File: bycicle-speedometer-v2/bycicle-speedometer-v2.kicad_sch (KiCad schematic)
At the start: 2 parts, among them J1 Conn_01x04_Pin

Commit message: initiated schematic update
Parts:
- removed uP1: ProMini2, Pro mini:Pro_Mini, symbol j_ProcessorBoards:ProMini2
- added C1: C, symbol Device:C
- added R1, R2, R3, R4, R5: R, symbol Device:R
- added U1: ESP-12E, ESP8266:ESP-12E, symbol ESP8266:ESP-12E
- J1: footprint Display:Adafruit_SSD1306 -> Connector_PinSocket_2.54mm:PinSocket_1x04_P2.54mm_Vertical
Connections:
- new net GND: C1.2, R5.2, U1.9 (GND)

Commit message: modified schematic
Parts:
- removed R4: R, symbol Device:R
- added J2: Conn_01x02_Pin, symbol Connector:Conn_01x02_Pin
- added SW1: SW_Push_Dual, symbol Switch:SW_Push_Dual
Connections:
- net GND: now also J1.4 (Pin_4), J2.1 (Pin_1), SW1.1
- net at U1.1 (REST): now also R2.2, SW1.2
- net at U1.10 (GPIO15): now also R5.1
- net Prog: now reaches U1.12 (GPIO0)
- net Prog: now also R3.2, J2.2 (Pin_2)
- net SDA: now reaches U1.13 (GPIO4)
- net SDA: now also J1.1 (Pin_1)
- net SCL: now reaches U1.14 (GPIO5)
- net SCL: now also J1.2 (Pin_2)
- net at U1.3 (CH_PD): now also R1.2
- net at U1.8 (VCC): now also C1.1
- net VCC: now reaches R2.1
- net VCC: now also J1.3 (Pin_3), R1.1, R3.1
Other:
- moved on the sheet: C1, R1, R5

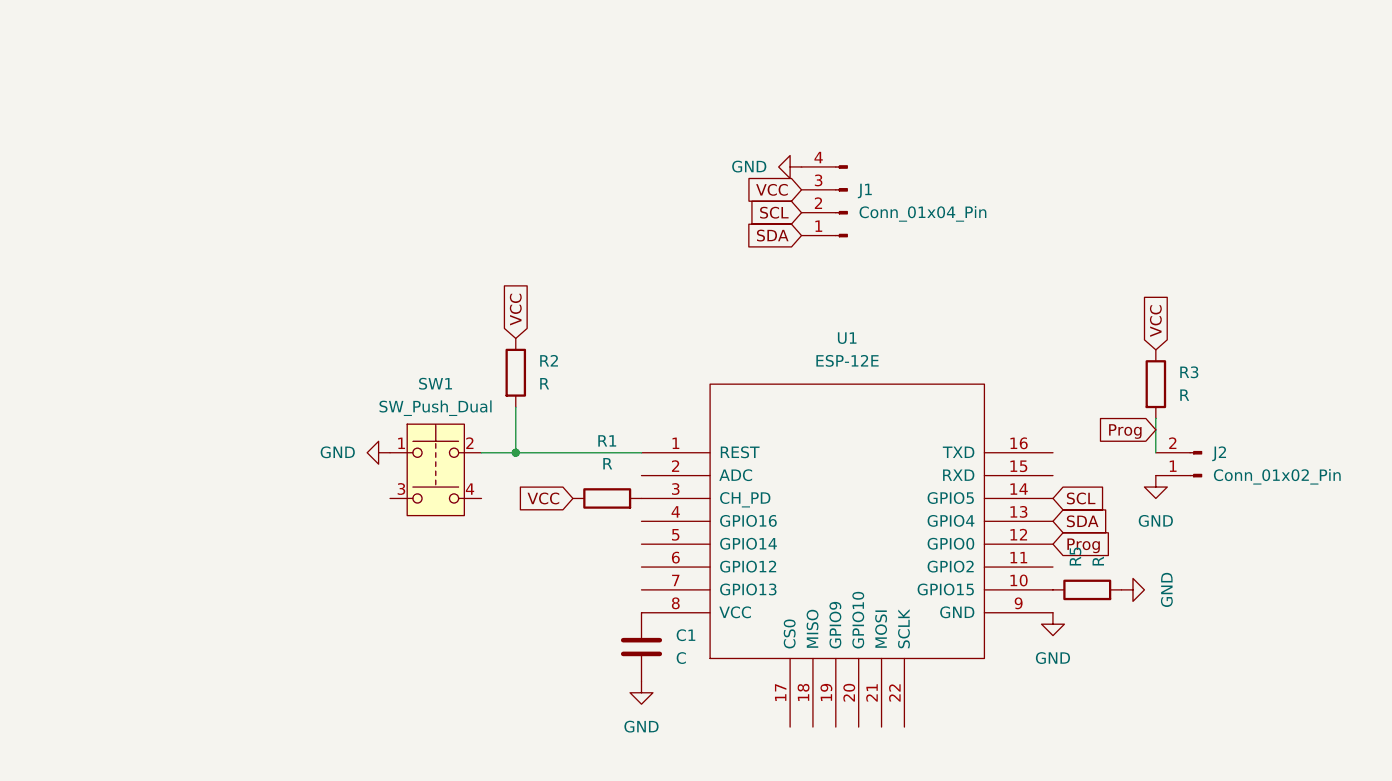
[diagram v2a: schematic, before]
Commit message: schematic edited a bit
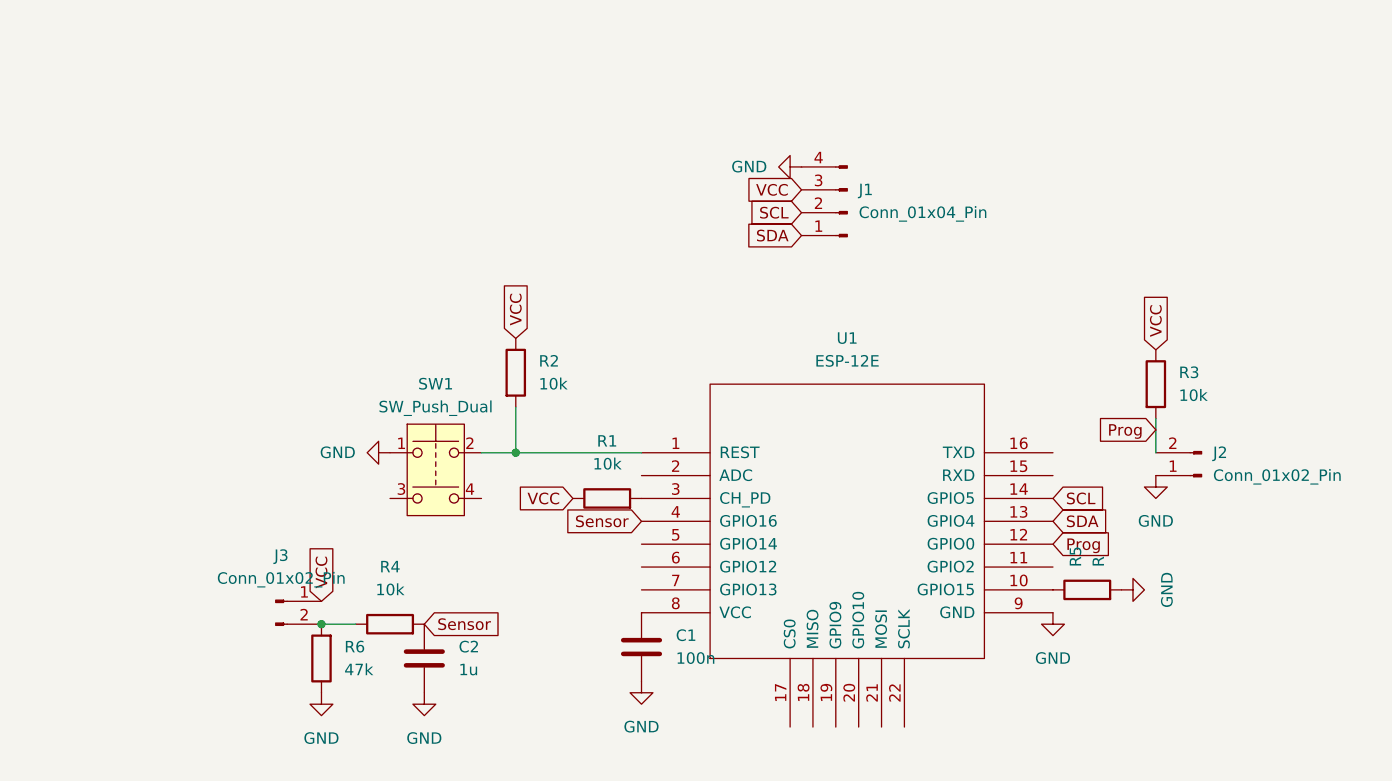
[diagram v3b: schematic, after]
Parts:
- added C2: 1u, Capacitor_SMD:C_0805_2012Metric, symbol Device:C
- added J3: Conn_01x02_Pin, Connector_PinHeader_2.54mm:PinHeader_1x02_P2.54mm_Vertical, symbol Connector:Conn_01x02_Pin
- added R4: 10k, Resistor_SMD:R_0805_2012Metric, symbol Device:R
- added R6: 47k, Resistor_SMD:R_0805_2012Metric, symbol Device:R
- C1: value C -> 100n; footprint (none) -> Capacitor_SMD:C_0805_2012Metric
- J2: footprint (none) -> Connector_PinHeader_2.54mm:PinHeader_1x02_P2.54mm_Vertical
- R1, R2, R3: value R -> 10k; footprint (none) -> Resistor_SMD:R_0805_2012Metric
- R5: footprint (none) -> Resistor_SMD:R_0805_2012Metric
- SW1: footprint (none) -> Button_Switch_THT:SW_PUSH_6mm
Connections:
- net GND: now also C2.2, R6.1
- net VCC: now also J3.1 (Pin_1)
- net Sensor: now reaches U1.4 (GPIO16)
- net Sensor: now also C2.1, R4.2
- new net: J3.2 (Pin_2), R4.1, R6.2

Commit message: schematic edited
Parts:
- removed J1: Conn_01x04_Pin, Connector_PinSocket_2.54mm:PinSocket_1x04_P2.54mm_Vertical, symbol Connector:Conn_01x04_Pin
- added U2: AMS1117-3.3, Package_TO_SOT_SMD:SOT-223-3_TabPin2, symbol Regulator_Linear:AMS1117-3.3
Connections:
- net GND: now also U2.1 (GND)
- net VCC: now also U2.3 (VI); no longer J3.1 (Pin_1), R1.1, R2.1, R3.1
- new net 3V3: J3.1 (Pin_1), R1.1, R2.1, R3.1, U2.2 (VO)
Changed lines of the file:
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@@
+	(wire
+		(pts
+			(xy 88.9 54.61) (xy 82.55 54.61)
+		)
+		(stroke
+			(width 0)
+			(type default)
+		)
+	)
 	(wire
 		(pts
@@
 		)
 	)
+	(wire
+		(pts
+			(xy 60.96 54.61) (xy 67.31 54.61)
+		)
+		(stroke
+			(width 0)
+			(type default)
+		)
+	)
 	(global_label "SCL"
 		(shape input)
@@
 		)
 	)
-	(global_label "VCC"
+	(global_label "3V3"
 		(shape input)
 		(at 173.99 72.39 90)
@@
 		)
 		(property "Intersheetrefs" "${INTERSHEET_REFS}"
-			(at 173.99 65.7762 90)
+			(at 173.99 65.8972 90)
 			(effects
 				(font
@@
 		)
 	)
-	(global_label "VCC"
+	(global_label "3V3"
 		(shape input)
 		(at 102.87 71.12 90)
@@
 		)
 		(property "Intersheetrefs" "${INTERSHEET_REFS}"
-			(at 102.87 64.5062 90)
+			(at 102.87 64.6272 90)
+			(effects
+				(font
+					(size 1.27 1.27)
+				)
+				(justify left)
+				(hide yes)
+			)
+		)
+	)
+	(global_label "3V3"
+		(shape input)
+		(at 88.9 54.61 0)
+		(fields_autoplaced yes)
+		(effects
+			(font
+				(size 1.27 1.27)
+			)
+			(justify left)
+		)
+		(property "Intersheetrefs" "${INTERSHEET_REFS}"
+			(at 95.3928 54.61 0)
 			(effects
 				(font
@@
 		)
 	)
-	(global_label "SDA"
+	(global_label "Prog"
 		(shape input)
-		(at 134.62 59.69 180)
+		(at 162.56 93.98 0)
 		(fields_autoplaced yes)
 		(effects
@@
 				(size 1.27 1.27)
 			)
-			(justify right)
+			(justify left)
 		)
 		(property "Intersheetrefs" "${INTERSHEET_REFS}"
-			(at 128.0667 59.69 0)
-			(effects
-				(font
-					(size 1.27 1.27)
-				)
-				(justify right)
-				(hide yes)
-			)
-		)
-	)
-	(global_label "Prog"
+			(at 169.8994 93.98 0)
+			(effects
+				(font
+					(size 1.27 1.27)
+				)
+				(justify left)
+				(hide yes)
+			)
+		)
+	)
+	(global_label "3V3"
 		(shape input)
-		(at 162.56 93.98 0)
+		(at 81.28 100.33 90)
 		(fields_autoplaced yes)
 		(effects
@@
 		)
 		(property "Intersheetrefs" "${INTERSHEET_REFS}"
-			(at 169.8994 93.98 0)
+			(at 81.28 93.8372 90)
 			(effects
 				(font
@@
 	(global_label "VCC"
 		(shape input)
-		(at 81.28 100.33 90)
+		(at 60.96 54.61 180)
 		(fields_autoplaced yes)
 		(effects
@@
 				(size 1.27 1.27)
 			)
-			(justify left)
+			(justify right)
 		)
 		(property "Intersheetrefs" "${INTERSHEET_REFS}"
-			(at 81.28 93.7162 90)
-			(effects
-				(font
-					(size 1.27 1.27)
-				)
-				(justify left)
+			(at 54.3462 54.61 0)
+			(effects
+				(font
+					(size 1.27 1.27)
+				)
+				(justify right)
 				(hide yes)
 			)
@@
 		)
 	)
-	(global_label "VCC"
+	(global_label "3V3"
 		(shape input)
 		(at 109.22 88.9 180)
@@
 		)
 		(property "Intersheetrefs" "${INTERSHEET_REFS}"
-			(at 102.6062 88.9 0)
-			(effects
-				(font
-					(size 1.27 1.27)
-				)
-				(justify right)
-				(hide yes)
-			)
-		)
-	)
-	(global_label "SCL"
-		(shape input)
-		(at 134.62 57.15 180)
-		(fields_autoplaced yes)
-		(effects
-			(font
-				(size 1.27 1.27)
-			)
-			(justify right)
-		)
-		(property "Intersheetrefs" "${INTERSHEET_REFS}"
-			(at 128.1272 57.15 0)
-			(effects
-				(font
-					(size 1.27 1.27)
-				)
-				(justify right)
-				(hide yes)
-			)
-		)
-	)
-	(global_label "VCC"
-		(shape input)
-		(at 134.62 54.61 180)
-		(fields_autoplaced yes)
-		(effects
-			(font
-				(size 1.27 1.27)
-			)
-			(justify right)
-		)
-		(property "Intersheetrefs" "${INTERSHEET_REFS}"
-			(at 128.0062 54.61 0)
+			(at 102.7272 88.9 0)
 			(effects
 				(font
@@
 	)
 	(symbol
-		(lib_id "power:GND")
-		(at 134.62 52.07 270)
-		(unit 1)
-		(exclude_from_sim no)
-		(in_bom yes)
-		(on_board yes)
-		(dnp no)
-		(fields_autoplaced yes)
-		(property "Reference" "#PWR06"
-			(at 128.27 52.07 0)
-			(effects
-				(font
-					(size 1.27 1.27)
-				)
-				(hide yes)
-			)
-		)
-		(property "Value" "GND"
-			(at 130.81 52.0699 90)
-			(effects
-				(font
-					(size 1.27 1.27)
-				)
-				(justify right)
-			)
-		)
-		(property "Footprint" ""
-			(at 134.62 52.07 0)
-			(effects
-				(font
-					(size 1.27 1.27)
-				)
-				(hide yes)
-			)
-		)
-		(property "Datasheet" ""
-			(at 134.62 52.07 0)
-			(effects
-				(font
-					(size 1.27 1.27)
-				)
-				(hide yes)
-			)
-		)
-		(property "Description" "Power symbol creates a global label with name \"GND\" , ground"
-			(at 134.62 52.07 0)
-			(effects
-				(font
-					(size 1.27 1.27)
-				)
-				(hide yes)
-			)
-		)
-		(pin "1"
-		)
-		(instances
-			(project "bycicle-speedometer-v2"
-				(path "/cd1ae02e-5075-48fd-aeda-d7bc106d32bf"
-					(reference "#PWR06")
-					(unit 1)
-				)
-			)
-		)
-	)
-	(symbol
 		(lib_id "Device:R")
 		(at 173.99 76.2 0)
@@
 	(symbol
 		(lib_id "power:GND")
+		(at 74.93 62.23 0)
+		(unit 1)
+		(exclude_from_sim no)
+		(in_bom yes)
+		(on_board yes)
+		(dnp no)
+		(fields_autoplaced yes)
+		(property "Reference" "#PWR06"
+			(at 74.93 68.58 0)
+			(effects
+				(font
+					(size 1.27 1.27)
+				)
+				(hide yes)
+			)
+		)
+		(property "Value" "GND"
+			(at 74.93 67.31 0)
+			(effects
+				(font
+					(size 1.27 1.27)
+				)
+			)
+		)
+		(property "Footprint" ""
+			(at 74.93 62.23 0)
+			(effects
+				(font
+					(size 1.27 1.27)
+				)
+				(hide yes)
+			)
+		)
+		(property "Datasheet" ""
+			(at 74.93 62.23 0)
+			(effects
+				(font
+					(size 1.27 1.27)
+				)
+				(hide yes)
+			)
+		)
+		(property "Description" "Power symbol creates a global label with name \"GND\" , ground"
+			(at 74.93 62.23 0)
+			(effects
+				(font
+					(size 1.27 1.27)
+				)
+				(hide yes)
+			)
+		)
+		(pin "1"
+		)
+		(instances
+			(project "bycicle-speedometer-v2"
+				(path "/cd1ae02e-5075-48fd-aeda-d7bc106d32bf"
+					(reference "#PWR06")
+					(unit 1)
+				)
+			)
+		)
+	)
+	(symbol
+		(lib_id "power:GND")
 		(at 173.99 86.36 0)
 		(unit 1)
@@
 	)
 	(symbol
-		(lib_id "Connector:Conn_01x04_Pin")
-		(at 139.7 57.15 180)
-		(unit 1)
-		(exclude_from_sim no)
-		(in_bom yes)
-		(on_board yes)
-		(dnp no)
-		(fields_autoplaced yes)
-		(property "Reference" "J1"
-			(at 140.97 54.6099 0)
-			(effects
-				(font
-					(size 1.27 1.27)
-				)
-				(justify right)
-			)
-		)
-		(property "Value" "Conn_01x04_Pin"
-			(at 140.97 57.1499 0)
-			(effects
-				(font
-					(size 1.27 1.27)
-				)
-				(justify right)
-			)
-		)
-		(property "Footprint" "Connector_PinSocket_2.54mm:PinSocket_1x04_P2.54mm_Vertical"
-			(at 139.7 57.15 0)
-			(effects
-				(font
-					(size 1.27 1.27)
-				)
-				(hide yes)
-			)
-		)
-		(property "Datasheet" "~"
-			(at 139.7 57.15 0)
-			(effects
-				(font
-					(size 1.27 1.27)
-				)
-				(hide yes)
-			)
-		)
-		(property "Description" "Generic connector, single row, 01x04, script generated"
-			(at 139.7 57.15 0)
-			(effects
-				(font
-					(size 1.27 1.27)
-				)
-				(hide yes)
-			)
+		(lib_id "Regulator_Linear:AMS1117-3.3")
+		(at 74.93 54.61 0)
+		(unit 1)
+		(exclude_from_sim no)
+		(in_bom yes)
+		(on_board yes)
+		(dnp no)
+		(fields_autoplaced yes)
+		(property "Reference" "U2"
+			(at 74.93 48.26 0)
+			(effects
+				(font
+					(size 1.27 1.27)
+				)
+			)
+		)
+		(property "Value" "AMS1117-3.3"
+			(at 74.93 50.8 0)
+			(effects
+				(font
+					(size 1.27 1.27)
+				)
+			)
+		)
+		(property "Footprint" "Package_TO_SOT_SMD:SOT-223-3_TabPin2"
+			(at 74.93 49.53 0)
+			(effects
+				(font
+					(size 1.27 1.27)
+				)
+				(hide yes)
+			)
+		)
+		(property "Datasheet" "http://www.advanced-monolithic.com/pdf/ds1117.pdf"
+			(at 77.47 60.96 0)
+			(effects
+				(font
+					(size 1.27 1.27)
+				)
+				(hide yes)
+			)
+		)
+		(property "Description" "1A Low Dropout regulator, positive, 3.3V fixed output, SOT-223"
+			(at 74.93 54.61 0)
+			(effects
+				(font
+					(size 1.27 1.27)
+				)
+				(hide yes)
+			)
+		)
+		(pin "3"
 		)
 		(pin "2"
 		)
-		(pin "3"
-		)
-		(pin "1"
-		)
-		(pin "4"
-		)
-		(instances
-			(project "bycicle-speedometer-v2"
-				(path "/cd1ae02e-5075-48fd-aeda-d7bc106d32bf"
-					(reference "J1")
-					(unit 1)
-				)
+		(pin "1"
+		)
+		(instances
+			(project "bycicle-speedometer-v2"
+				(path "/cd1ae02e-5075-48fd-aeda-d7bc106d32bf"
+					(reference "U2")
+					(unit 1)
+				)

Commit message: edited schematic diagram
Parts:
- added C3, C4: 10u, Capacitor_SMD:CP_Elec_5x4.5, symbol Device:C_Polarized
- added D1, D2, D3, D4, D5, D6: LED, LED_THT:LED_D5.0mm, symbol Device:LED
- added J1: Conn_01x02_Pin, TerminalBlock_Phoenix:TerminalBlock_Phoenix_MKDS-1,5-2-5.08_1x02_P5.08mm_Horizontal, symbol Connector:Conn_01x02_Pin
- added R7, R8, R9: 10k, Resistor_SMD:R_0805_2012Metric, symbol Device:R
- J3: footprint Connector_PinHeader_2.54mm:PinHeader_1x02_P2.54mm_Vertical -> TerminalBlock_Phoenix:TerminalBlock_Phoenix_MKDS-1,5-2-5.08_1x02_P5.08mm_Horizontal
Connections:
- net 3V3: now also C4.1
- net GND: now also C3.2, C4.2, J1.2 (Pin_2)
- net VCC: now also C3.1, J1.1 (Pin_1)
- net led_a: now reaches U1.5 (GPIO14)
- net led_a: now also R7.1
- net led_b: now reaches U1.6 (GPIO12)
- net led_b: now also R8.1
- net led_c: now reaches U1.7 (GPIO13)
- net led_c: now also R9.1
- net SCL: no longer names the net of U1.14 (GPIO5)
- net SDA: no longer names the net of U1.13 (GPIO4)
- new net: D1.2 (A), D2.1 (K), D5.2 (A), D6.1 (K), R7.2
- new net: D3.1 (K), D4.2 (A), D5.1 (K), D6.2 (A), R9.2
- new net: D1.1 (K), D2.2 (A), D3.2 (A), D4.1 (K), R8.2

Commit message: edited schematics
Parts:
- removed C3, C4: 10u, Capacitor_SMD:CP_Elec_5x4.5, symbol Device:C_Polarized
- removed U2: AMS1117-3.3, Package_TO_SOT_SMD:SOT-223-3_TabPin2, symbol Regulator_Linear:AMS1117-3.3
- added J4: Conn_01x03_Pin, Connector_PinHeader_2.54mm:PinHeader_1x03_P2.54mm_Vertical, symbol Connector:Conn_01x03_Pin
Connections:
- net 3V3: now also J4.1 (Pin_1)
- net GND: now also J4.2 (Pin_2)
- net VCC: now also J4.3 (Pin_3)
